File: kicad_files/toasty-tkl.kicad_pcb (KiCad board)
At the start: 2 copper layers, 345.7 x 134.1 mm, 204 parts, among them CON1 USB-MINI-B, Q1 FET_N, SW0:0 ESC, SW0:10 F9, SW0:11 F10, SW0:12 F11, SW0:13 F12, SW0:14 PRINT, SW0:15 SCROLL LOCK, SW0:2 F1, SW0:3 F2, SW0:4 F3, SW0:5 F4, SW0:6 F5, SW0:7 F6, SW0:8 F7, SW0:9 F8, SW1:0 `, SW1:1 1, SW1:10 0, SW1:11 -, SW1:12 =, SW1:13 BACK SPACE, SW1:14 INSERT, SW1:15 HOME, SW1:2 2, SW1:3 3, SW1:4 4, SW1:5 5, SW1:6 6, SW1:7 7, SW1:8 8, SW1:9 9, SW2:0 TAB, SW2:1 Q, SW2:10 P, SW2:11 [, SW2:12 ], SW2:13 \, SW2:14 DELETE, SW2:15 END, SW2:2 W, SW2:3 E, SW2:4 R, SW2:5 T, SW2:6 Y, SW2:7 U, SW2:8 I, SW2:9 O, SW3:0 CAPS LOCK, SW3:1 A, SW3:10 ;, SW3:11 ', SW3:13 ENTER, SW3:14 PAGE UP, SW3:15 PAUSE, SW3:2 S, SW3:3 D, SW3:4 F, SW3:5 G, SW3:6 H, SW3:7 J, SW3:8 K, SW3:9 L, SW4:0 LEFT SHIFT, SW4:1 Z, SW4:10 /, SW4:13 RIGHT SHIFT, SW4:14 PAGE DOWN, SW4:15 UP, SW4:2 X, SW4:3 C, SW4:4 V, SW4:5 B, SW4:6 N, SW4:7 M, SW4:8 ,, SW4:9 ., SW5:0 LEFT CTRL, SW5:1 LEFT WINDOWS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

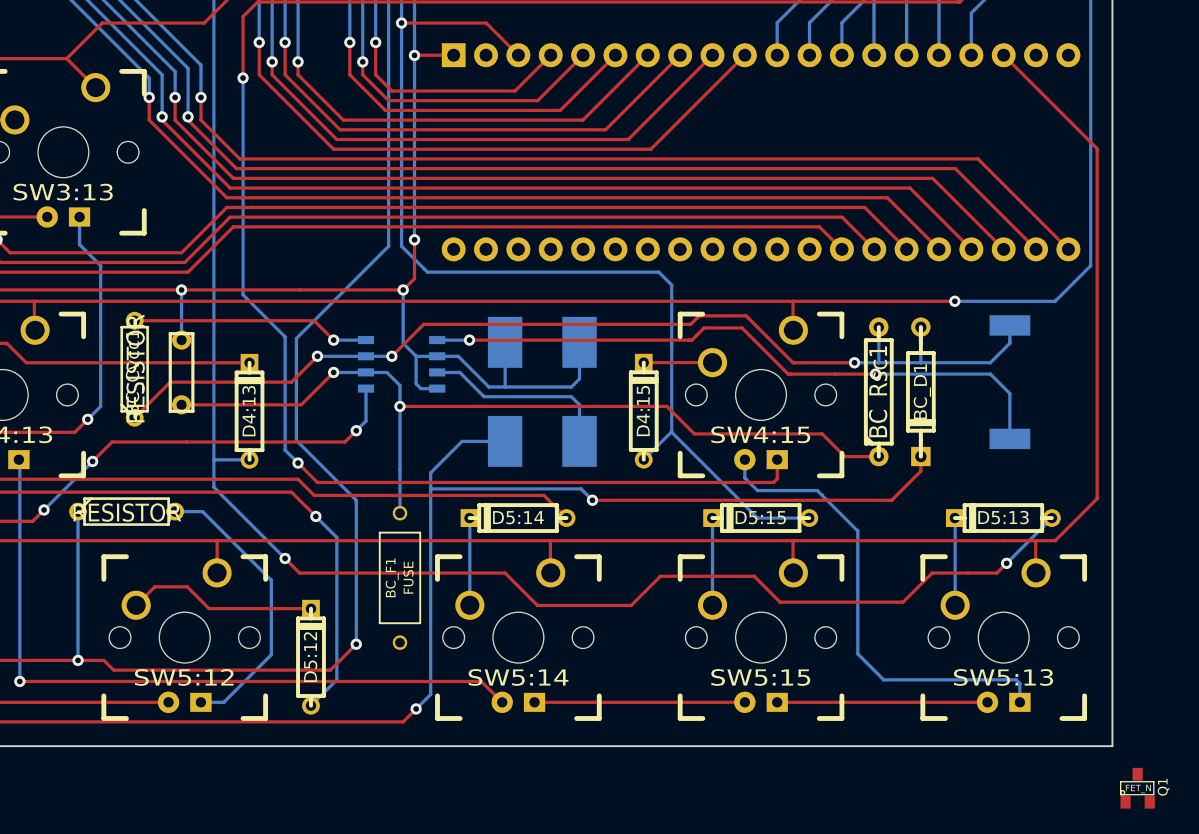
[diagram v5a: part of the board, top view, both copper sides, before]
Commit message: Small trace adjustments on boost converter.  Needs review, changes, thicker wires, cleanup, fixing of labels... : (
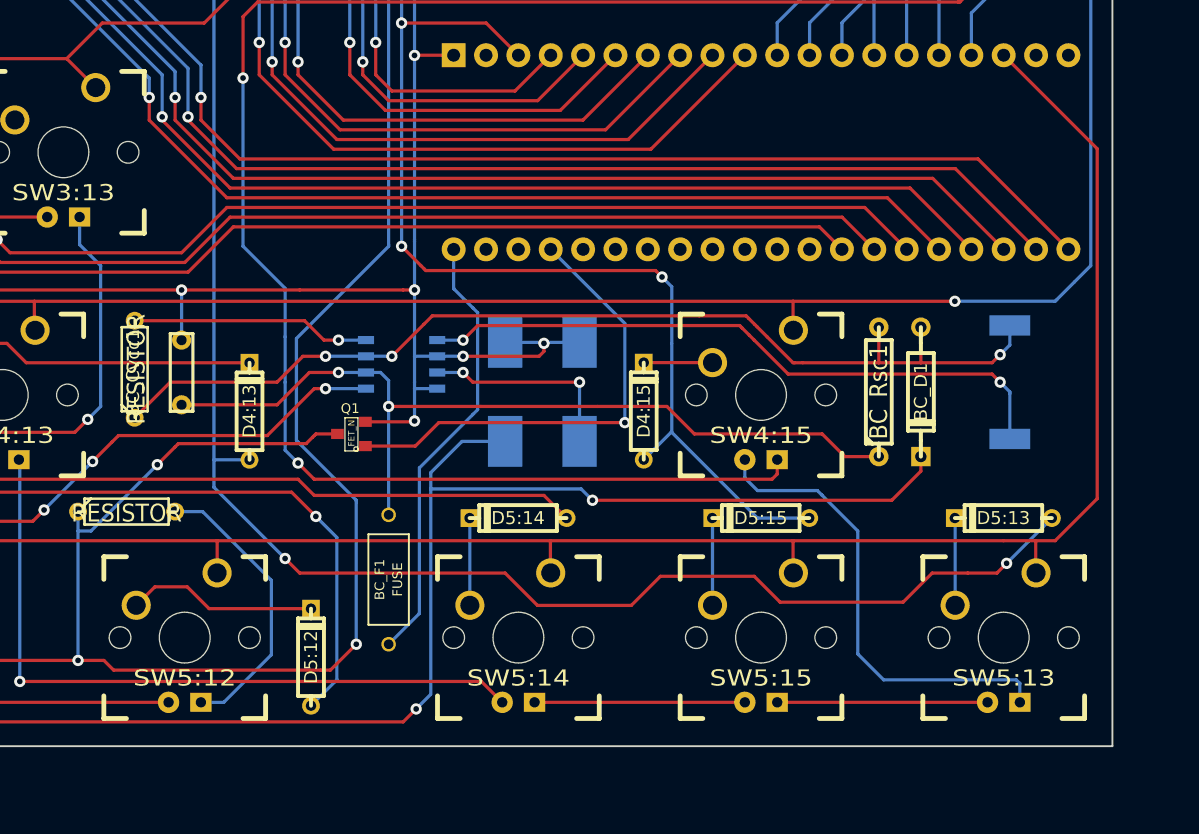
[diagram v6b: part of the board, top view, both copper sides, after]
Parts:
- moved Q1 67.7 mm to (304.4, 115.1), turned to 90 degrees
- moved BC_F1 0.90 mm to (307.3, 126.5)
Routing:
- net N-0000097: track 0.00 -> 37.1 mm, vias 0 -> 1
- net N-0000094: track 0.00 -> 34.7 mm
- net N-0000071: track 310.6 -> 334.1 mm, vias 4 -> 5
- net /GND: track 182.2 -> 185.3 mm, vias 6 -> 8
- net N-0000090: track 67.0 -> 65.5 mm
- net N-0000091: track 15.1 -> 16.1 mm, vias 0 -> 2
- net /COL 15: track 197.9 -> 197.8 mm, vias 6 -> 8

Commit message: Thickened all 10 mil vcc and gnd traces to 20mm and reogranised.
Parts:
- moved BC_Cvcc1 20.8 mm to (280.7, 128.3)
- moved BC_R0 16.7 mm to (301.8, 101.5), turned to 0 degrees
- moved BC_R1 7.80 mm to (256.5, 102.5)
- moved BC_R2 7.39 mm to (256.5, 106.3)
- moved VREG1 2.67 mm to (305.7, 109.6)
- moved Q1 0.76 mm to (304.4, 115.8)
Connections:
- R12 pad 1: (no net) -> N-0000071
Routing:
- net N-0000071: track 334.1 -> 294.8 mm
- net N-0000092: track 68.2 -> 85.8 mm, vias 2 -> 3
- net /GND: track 185.3 -> 200.2 mm, vias 8 -> 5
- net N-00000100: track 18.8 -> 7.33 mm, vias 1 -> 0
- net /LEDCOL0: track 715.9 -> 726.5 mm, vias 6 -> 8
- net N-0000090: track 65.5 -> 72.9 mm
- net /LEDROW0: track 131.3 -> 138.2 mm
- net /LEDROW1: track 82.5 -> 76.1 mm
- net N-00000178: track 42.2 -> 36.8 mm
- net N-0000099: track 81.2 -> 77.1 mm, vias 3 -> 2
- net N-0000089: track 136.1 -> 139.5 mm
- net /LEDROW10: track 60.2 -> 62.4 mm, vias 1 -> 0
- net /ROW 4: track 398.7 -> 400.8 mm, vias 1 -> 2
- net /LEDROW2: track 58.4 -> 56.5 mm
- net /COL 13: track 295.9 -> 297.8 mm
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
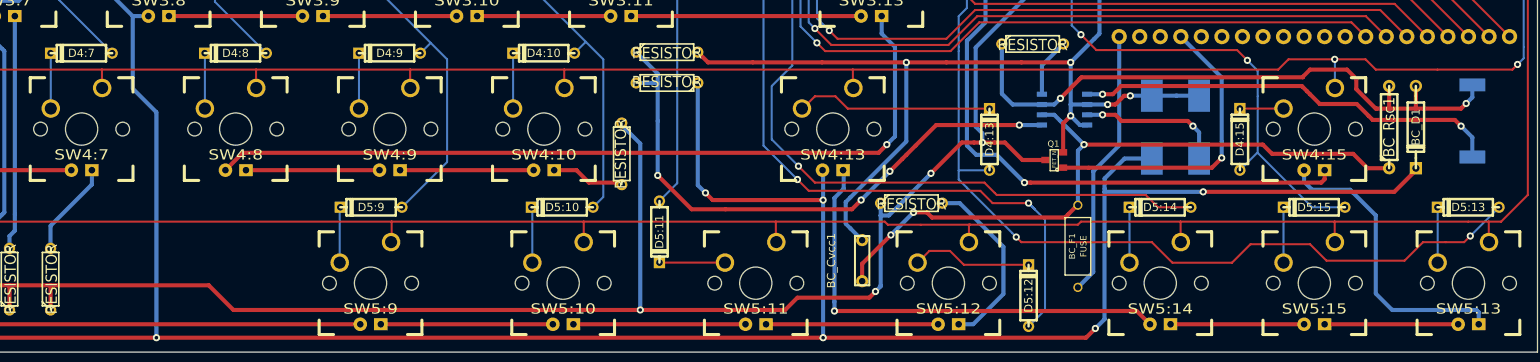
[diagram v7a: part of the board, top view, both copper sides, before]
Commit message: Swapped Two Capacitors I had swapped earlier by accident.  Rewired them.  Split parts list away from led notes.
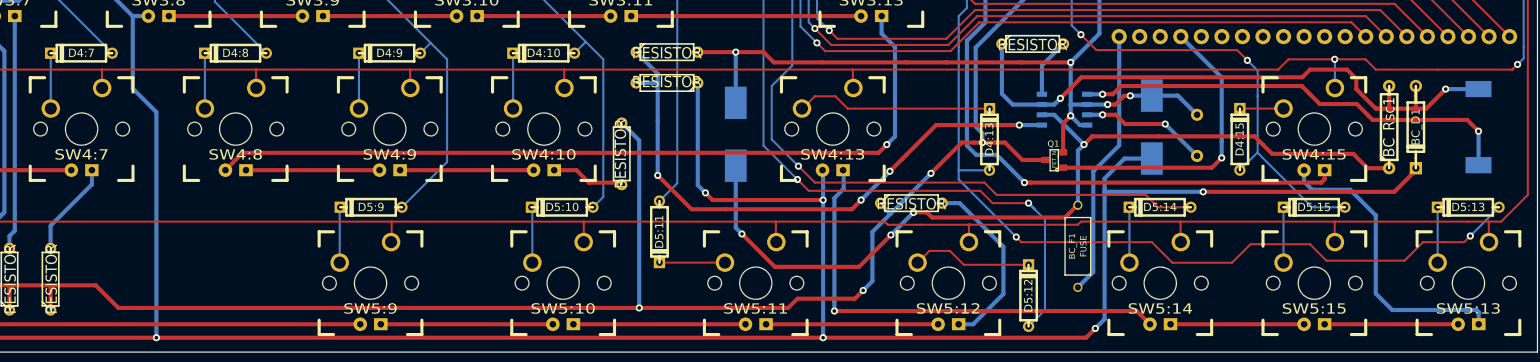
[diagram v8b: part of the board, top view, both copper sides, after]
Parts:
- BC_Ct1: footprint TantalC_SizeD_EIA-7343_HandSoldering_RevA_28Aug2012 -> CP_6mm
- BC_Cvcc1: footprint CP_6mm -> TantalC_SizeD_EIA-7343_HandSoldering_RevA_28Aug2012; moved to B.Cu
- moved BC_Cvcc1 22.1 mm to (265.0, 112.6)
- moved BC_L1 1.08 mm to (356.9, 111.8)
- moved BC_Ct1 1.05 mm to (322.1, 112.8)
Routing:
- net N-0000092: track 85.8 -> 110.0 mm, vias 3 -> 4
- net /GND: track 200.2 -> 181.2 mm
- net N-0000091: track 18.0 -> 15.7 mm
- net N-0000098: track 53.1 -> 55.3 mm
- net N-0000071: track 294.8 -> 293.3 mm
